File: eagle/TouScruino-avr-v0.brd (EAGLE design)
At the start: 63.5 x 73.7 mm, 47 parts, among them J1 AVR_ISP, Q1 8MHz, Q2 MMBT2222A, Q3 8MHz, U1 ATMEGA1284P, U3 ARDUINO_SHIELD, U4 MCP73831, U5 MIC5209-3.3YS, X2 USB-MICROB

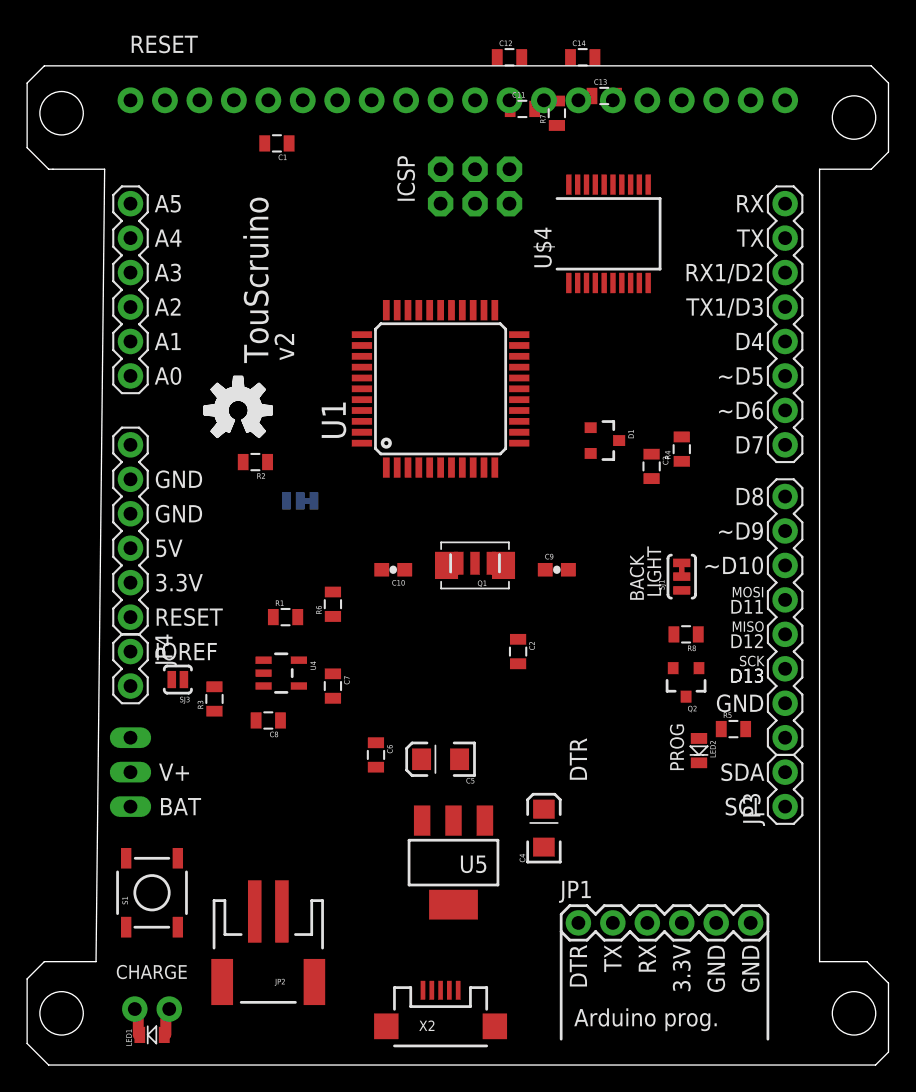
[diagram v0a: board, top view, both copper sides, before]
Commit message: 
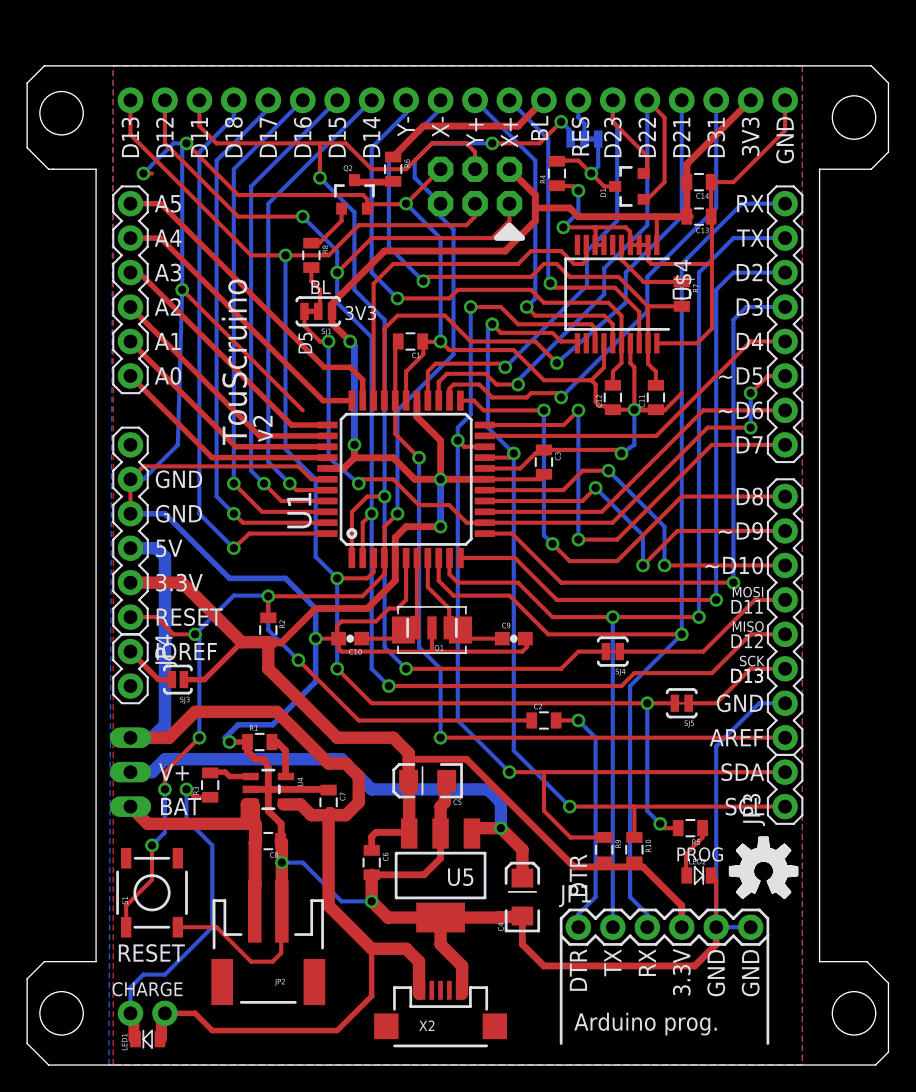
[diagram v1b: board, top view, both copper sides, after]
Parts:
- added R10: 4K7, SparkFun:0805
- added R9: 4k7, SparkFun:0805
- added SJ4, SJ5: (no value), SparkFun:SJ_2S-TRACE
- U$6: device wibauxl:1X20 -> wibauxl:TFT_20
- moved U$3 51.5 mm to (54.3, 14.3)
- moved U$5 51.5 mm to (54.3, 14.3)
- moved Q2 43.4 mm to (24.1, 64.1), turned to 0 degrees
- moved R8 39.3 mm to (21.0, 59.7), turned to 270 degrees
- moved SJ2 33.9 mm to (41.6, 68.3)
- moved SJ1 33.3 mm to (21.0, 55.6), turned to 180 degrees
- moved R6 32.4 mm to (27.0, 66.0), turned to 270 degrees
- moved C12 26.2 mm to (43.2, 49.2), turned to 90 degrees
- moved C11 23.4 mm to (46.4, 49.2), turned to 90 degrees
- moved R4 22.3 mm to (39.1, 65.7)
- moved D1 18.8 mm to (44.5, 64.8), turned to 90 degrees
- moved C1 17.6 mm to (28.3, 53.3)
- moved R7 16.2 mm to (48.3, 56.8), turned to 270 degrees
- moved C14 12.6 mm to (49.5, 65.1), turned to 180 degrees
- moved R2 12.4 mm to (17.8, 32.1), turned to 270 degrees
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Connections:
- new net N$10: SJ5.1, U3.D13
- new net N$3: SJ4.1, U3.D11
- net 3.3V: now also R10.2, R9.2
- net A7/D31: now also U$6.17; no longer U$6.15
- net AREF: now also U3.AREF
- net D11/MOSI: now also SJ4.2; no longer U3.D11
- net D13/SCK: now also SJ5.2; no longer U3.D13
- net D19/SCL: now also R10.1
- net D20/SDA: now also R9.1
- net D22: now also D1.1, U$6.16; no longer D1.2, U$6.17
- net D23: now also D1.2, U$6.15; no longer D1.1, U$6.16
- net VUSB: now also JP5.3
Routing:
- net GND: track 0.00 -> 371.0 mm, vias 0 -> 13
- net 3.3V: track 0.00 -> 181.0 mm, vias 0 -> 4
- net RES: track 0.00 -> 119.2 mm, vias 0 -> 9
- net D13/SCK: track 0.00 -> 106.4 mm, vias 0 -> 5
- net D12/MISO: track 0.00 -> 102.7 mm, vias 0 -> 4
- net D11/MOSI: track 0.00 -> 88.8 mm, vias 0 -> 3
- net VUSB: track 0.00 -> 85.1 mm
- net D0/RX: track 0.00 -> 81.7 mm, vias 0 -> 1
- net D20/SDA: track 0.00 -> 77.8 mm, vias 0 -> 3
- net D1/TX: track 0.00 -> 76.6 mm, vias 0 -> 2
- net D19/SCL: track 0.00 -> 65.5 mm, vias 0 -> 3
- net AREF: track 0.00 -> 56.1 mm, vias 0 -> 2
- net D5/PWM1: track 0.00 -> 53.7 mm, vias 0 -> 4
- net D2/RX1: track 0.00 -> 48.6 mm, vias 0 -> 1
- net D3/TX1: track 0.00 -> 43.4 mm, vias 0 -> 1
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- added copper zone on layer 1, net GND
- added copper zone on layer 16, net GND
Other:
- outline, holes or cut-outs redrawn
- board text added: "3V3"
- board text added: "AREF"
- board text added: "BL"
- board text added: "D14"
- board text added: "D15"
- board text added: "D16"
- board text added: "D17"
- board text added: "D18"
- board text added: "D2"
- board text added: "D21"
- board text added: "D22"
- board text added: "D23"
- board text added: "D3"
- board text added: "D31"
- board text added: "D5"
- board text added: "RES"
- board text added: "X+"
- board text added: "X-"
- board text added: "Y+"
- board text added: "Y-"
- board text removed: "BACK"
- board text removed: "ICSP"
- board text removed: "LIGHT"
- board text removed: "RX1/D2"
- board text removed: "TX1/D3"

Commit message: 
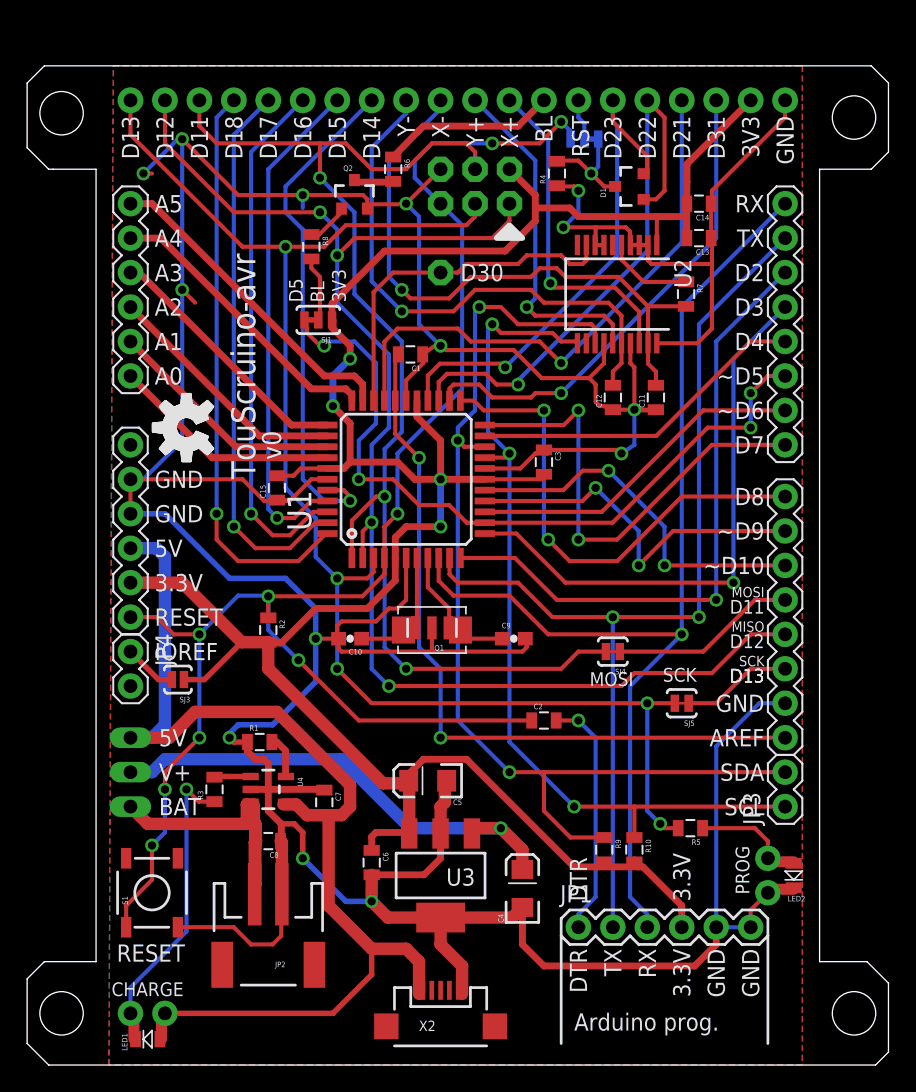
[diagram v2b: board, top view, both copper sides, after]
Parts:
- removed U5: MIC5209-3.3YS, wibauxl:SOT223
- added C15: 0.1uF, SparkFun:0805
- added JP7: ARDUINO_SHIELD, wibauxl:ARDUINO_SHIELD
- added JP8: M01, wibauxl:1X1
- LED2: device wibauxl:LED-0805 -> wibauxl:LED
- U2: value AR1020 -> AR1021
- U3: value ARDUINO_SHIELD -> MIC5209-3.3YS; device wibauxl:ARDUINO_SHIELD -> wibauxl:SOT223
- moved U3 61.3 mm to (30.5, 14.0), flipped to the top, turned to 180 degrees
- moved U$3 53.7 mm to (11.7, 47.0), turned to 90 degrees
- moved U$5 53.7 mm to (11.7, 47.0), turned to 90 degrees
- moved LED2 6.98 mm to (56.5, 14.0), turned to 270 degrees
- moved C14 1.59 mm to (49.5, 63.5)
- moved C13 1.59 mm to (49.5, 61.0)
- moved JP2 1.27 mm to (17.8, 8.89)
- moved C1 0.95 mm to (28.3, 52.4)
- moved R8 0.64 mm to (21.0, 60.3)
- moved C4 0.63 mm to (36.5, 13.0)
- moved SJ1 0.63 mm to (21.0, 54.9)
- moved R3 0.45 mm to (13.8, 20.3)
- moved C7 0.32 mm to (21.9, 19.4)
- moved R7 0.32 mm to (48.6, 56.8)
- renumbered U$4 to U2, U$6 to JP6
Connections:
- net 3.3V: now also C15.2, JP7.3.3V, U3.3; no longer U3.3.3V, U5.3
- net A0/D24: now also JP7.A0; no longer U3.A0
- net A1/D25: now also JP7.A1; no longer U3.A1
- net A2/D26: now also JP7.A2; no longer U3.A2
- net A3/D27: now also JP7.A3; no longer U3.A3
- net A4/D28: now also JP7.A4; no longer U3.A4
- net A5/D29: now also JP7.A5; no longer U3.A5
- net A6/D30: now also JP8.1
- net AREF: now also JP7.AREF; no longer U3.AREF
- net D0/RX: now also JP7.RX; no longer U3.RX
- net D1/TX: now also JP7.TX; no longer U3.TX
- net D10/PWM4: now also JP7.D10; no longer U3.D10
- net D12/MISO: now also JP7.D12; no longer U3.D12
- net D2/RX1: now also JP7.D2; no longer U3.D2
- net D3/TX1: now also JP7.D3; no longer U3.D3
- net D4: now also JP7.D4; no longer U3.D4
- net D5/PWM1: now also JP7.D5; no longer U3.D5
- net D6/PWM2: now also JP7.D6; no longer U3.D6
- net D7: now also JP7.D7; no longer U3.D7
- net D8: now also JP7.D8; no longer U3.D8
- net D9/PWM3: now also JP7.D9; no longer U3.D9
- net GND: now also C15.1, JP7.GND@0, JP7.GND@1, JP7.GND@2, LED2.C1, U3.2, U3.4; no longer LED2.2, U3.GND@0, U3.GND@1, U3.GND@2, U5.2, U5.4
- net N$10: now also JP7.D13; no longer U3.D13
- net N$3: now also JP7.D11; no longer U3.D11
- net N$5: now also LED2.A1; no longer LED2.1
- net RES: now also JP7.RES; no longer U3.RES
- net V+: now also U3.1; no longer U5.1
- net VUSB: now also JP7.5V; no longer U3.5V
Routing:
- net GND: track 371.0 -> 363.1 mm, vias 13 -> 14
- net X-: track 43.0 -> 45.7 mm
- net VBAT: track 27.7 -> 25.1 mm
- net N$5: track 4.02 -> 6.48 mm
- net D14: track 35.0 -> 37.4 mm
- net VUSB: track 85.1 -> 82.8 mm
- net D2/RX1: track 48.6 -> 46.4 mm
- net D1/TX: track 76.6 -> 74.3 mm
- net N$8: track 22.7 -> 20.7 mm
- net D0/RX: track 81.7 -> 79.8 mm
- net V+: track 37.6 -> 35.8 mm
- net D3/TX1: track 43.4 -> 41.7 mm
- net D5/PWM1: track 53.7 -> 55.1 mm
- net A7/D31: track 43.2 -> 41.9 mm
- net BL: track 3.89 -> 5.07 mm
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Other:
- board text added: "D30"
- board text added: "RST"
- board text added: "TouScruino-avr"
- board text added: "v0"
- board text removed: "RES"
- board text removed: "TouScruino"
- board text removed: "v2"

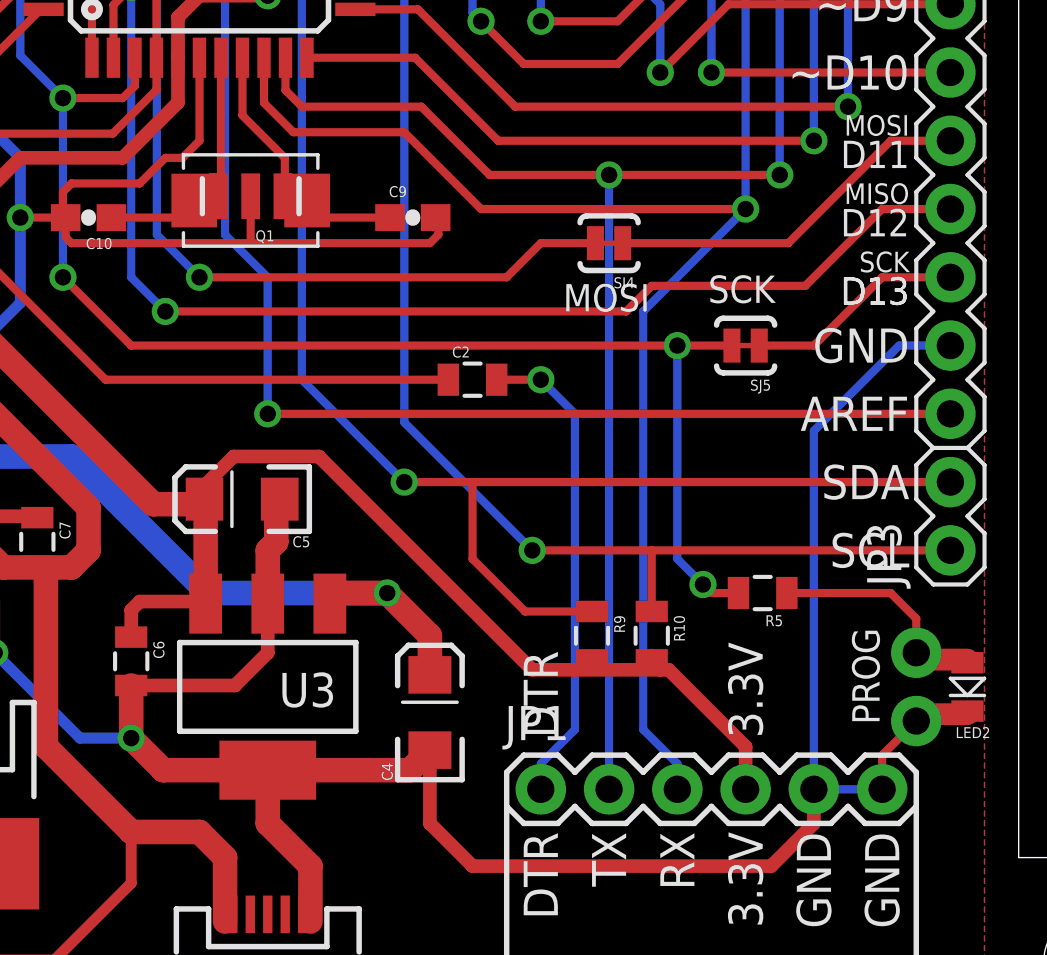
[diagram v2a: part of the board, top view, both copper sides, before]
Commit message: 
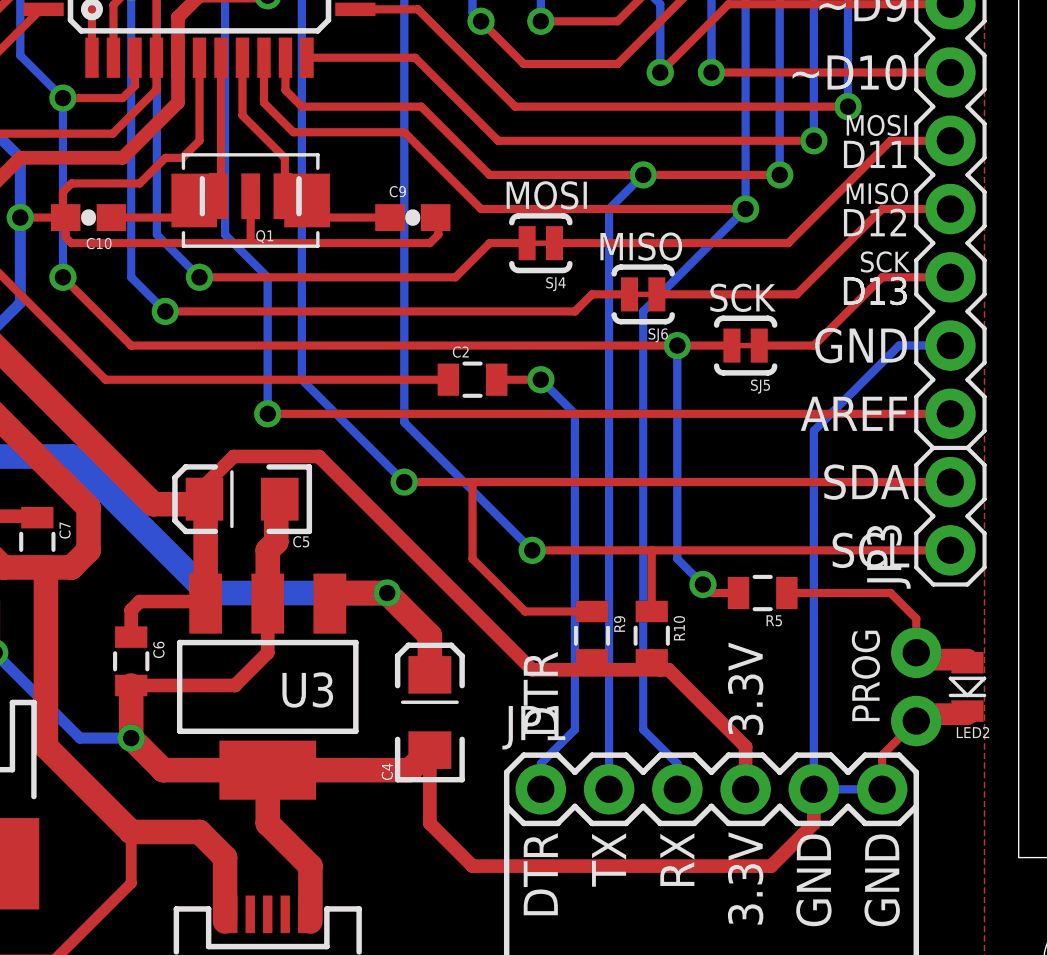
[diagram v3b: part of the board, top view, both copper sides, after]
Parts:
- added SJ6: (no value), SparkFun:SJ_2S-TRACE
- C13: value 100nF -> 0.1uF
- moved SJ4 2.54 mm to (40.6, 30.5)
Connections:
- new net N$14: JP7.D12, SJ6.1
- net D12/MISO: now also SJ6.2; no longer JP7.D12
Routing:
- net D12/MISO: track 103.5 -> 90.2 mm
- net N$14: track 0.00 -> 12.2 mm
- net N$3: track 13.8 -> 16.3 mm
- net D11/MOSI: track 89.4 -> 86.9 mm
- net D1/TX: track 74.3 -> 74.9 mm
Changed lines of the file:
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@@
 <text x="9.7155" y="23.495" size="1.27" layer="21" font="vector" ratio="15">5V</text>
 <text x="31.9405" y="57.785" size="1.27" layer="21" font="vector" ratio="15">D30</text>
-<text x="41.4655" y="27.94" size="1.016" layer="21" font="vector" ratio="12">MOSI</text>
-<text x="46.863" y="28.2575" size="1.016" layer="21" font="vector" ratio="12">SCK</text>
+<text x="39.243" y="31.75" size="1.016" layer="21" font="vector" ratio="12">MOSI</text>
+<text x="46.863" y="27.94" size="1.016" layer="21" font="vector" ratio="12">SCK</text>
+<text x="42.7355" y="29.845" size="1.016" layer="21" font="vector" ratio="12">MISO</text>
 </plain>
 <attributes>
@@
 <element name="C11" library="SparkFun" package="0805" value="10nF" x="46.355" y="49.2125" rot="R90"/>
 <element name="C12" library="SparkFun" package="0805" value="10nF" x="43.18" y="49.2125" rot="R90"/>
-<element name="C13" library="SparkFun" package="0805" value="100nF" x="49.53" y="60.96" rot="R180"/>
+<element name="C13" library="SparkFun" package="0805" value="0.1uF" x="49.53" y="60.96" rot="R180"/>
 <element name="C14" library="SparkFun" package="0805" value="10uF" x="49.53" y="63.5" rot="R180"/>
-<element name="SJ4" library="SparkFun" package="SJ_2S-TRACE" value="" x="43.18" y="30.48" rot="R180"/>
+<element name="SJ4" library="SparkFun" package="SJ_2S-TRACE" value="" x="40.64" y="30.48" rot="R180"/>
 <element name="SJ5" library="SparkFun" package="SJ_2S-TRACE" value="" x="48.26" y="26.67" rot="R180"/>
 <element name="JP6" library="wibauxl" package="TFT_20" value="TFT_20" x="7.62" y="71.12" rot="MR0"/>
@@
 <element name="JP8" library="wibauxl" package="1X1" value="M01" x="30.48" y="58.42"/>
 <element name="LED2" library="wibauxl" package="LED" value="Red" x="56.515" y="13.97" rot="R270"/>
+<element name="SJ6" library="SparkFun" package="SJ_2S-TRACE" value="" x="44.45" y="28.575" rot="R180"/>
 </elements>
 <signals>
@@
 <wire x1="31.75" y1="35.56" x2="36.195" y2="35.56" width="0.3048" layer="1"/>
 <wire x1="36.195" y1="35.56" x2="38.735" y2="33.02" width="0.3048" layer="1"/>
-<wire x1="49.53" y1="33.02" x2="43.18" y2="33.02" width="0.3048" layer="1"/>
-<wire x1="43.18" y1="33.02" x2="38.735" y2="33.02" width="0.3048" layer="1"/>
-<wire x1="43.18" y1="10.16" x2="43.18" y2="33.02" width="0.3048" layer="16"/>
-<via x="43.18" y="33.02" extent="1-16" drill="0.6096"/>
+<wire x1="49.53" y1="33.02" x2="44.45" y2="33.02" width="0.3048" layer="1"/>
+<wire x1="44.45" y1="33.02" x2="38.735" y2="33.02" width="0.3048" layer="1"/>
+<wire x1="43.18" y1="10.16" x2="43.18" y2="31.75" width="0.3048" layer="16"/>
+<wire x1="43.18" y1="31.75" x2="44.45" y2="33.02" width="0.3048" layer="16"/>
+<via x="44.45" y="33.02" extent="1-16" drill="0.6096"/>
 </signal>
 <signal name="N$5">
@@
 <wire x1="26.3525" y1="41.91" x2="26.3525" y2="30.7975" width="0.3048" layer="16"/>
 <wire x1="26.3525" y1="30.7975" x2="27.94" y2="29.21" width="0.3048" layer="16"/>
-<wire x1="27.94" y1="29.21" x2="39.37" y2="29.21" width="0.3048" layer="1"/>
-<wire x1="39.37" y1="29.21" x2="40.64" y2="30.48" width="0.3048" layer="1"/>
+<wire x1="27.94" y1="29.21" x2="37.465" y2="29.21" width="0.3048" layer="1"/>
+<wire x1="37.465" y1="29.21" x2="38.735" y2="30.48" width="0.3048" layer="1"/>
 <via x="27.94" y="29.21" extent="1-16" drill="0.6096"/>
-<wire x1="40.64" y1="30.48" x2="42.672" y2="30.48" width="0.3048" layer="1"/>
+<wire x1="38.735" y1="30.48" x2="40.132" y2="30.48" width="0.3048" layer="1"/>
 <wire x1="12.7" y1="69.215" x2="12.7" y2="71.12" width="0.3048" layer="1"/>
 </signal>
 <signal name="D12/MISO">
 <contactref element="U1" pad="2"/>
-<contactref element="JP7" pad="D12"/>
 <contactref element="J1" pad="1"/>
 <wire x1="10.16" y1="71.12" x2="10.16" y2="67.945" width="0.3048" layer="1"/>
@@
 <wire x1="25.4" y1="40.005" x2="25.4" y2="29.21" width="0.3048" layer="16"/>
 <wire x1="25.4" y1="29.21" x2="26.67" y2="27.94" width="0.3048" layer="16"/>
-<wire x1="26.67" y1="27.94" x2="43.815" y2="27.94" width="0.3048" layer="1"/>
-<wire x1="43.815" y1="27.94" x2="44.7675" y2="28.8925" width="0.3048" layer="1"/>
-<wire x1="44.7675" y1="28.8925" x2="50.4825" y2="28.8925" width="0.3048" layer="1"/>
-<wire x1="50.4825" y1="28.8925" x2="53.34" y2="31.75" width="0.3048" layer="1"/>
-<wire x1="53.34" y1="31.75" x2="55.88" y2="31.75" width="0.3048" layer="1"/>
+<wire x1="26.67" y1="27.94" x2="41.91" y2="27.94" width="0.3048" layer="1"/>
+<wire x1="41.91" y1="27.94" x2="42.545" y2="28.575" width="0.3048" layer="1"/>
 <via x="26.67" y="27.94" extent="1-16" drill="0.6096"/>
+<contactref element="SJ6" pad="2"/>
+<wire x1="43.942" y1="28.575" x2="42.545" y2="28.575" width="0.3048" layer="1"/>
 </signal>
 <signal name="D13/SCK">
@@
 <wire x1="55.88" y1="34.29" x2="53.6575" y2="34.29" width="0.3048" layer="1"/>
 <wire x1="53.6575" y1="34.29" x2="49.8475" y2="30.48" width="0.3048" layer="1"/>
-<wire x1="49.8475" y1="30.48" x2="43.688" y2="30.48" width="0.3048" layer="1"/>
+<wire x1="49.8475" y1="30.48" x2="41.148" y2="30.48" width="0.3048" layer="1"/>
 </signal>
 <signal name="N$10">
@@
 <wire x1="53.34" y1="29.21" x2="55.88" y2="29.21" width="0.3048" layer="1"/>
 </signal>
+<signal name="N$14">
+<contactref element="JP7" pad="D12"/>
+<contactref element="SJ6" pad="1"/>
+<wire x1="44.958" y1="28.575" x2="50.165" y2="28.575" width="0.3048" layer="1"/>
+<wire x1="50.165" y1="28.575" x2="53.34" y2="31.75" width="0.3048" layer="1"/>
+<wire x1="53.34" y1="31.75" x2="55.88" y2="31.75" width="0.3048" layer="1"/>
+</signal>
 </signals>
